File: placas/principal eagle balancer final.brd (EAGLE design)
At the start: 100 x 151 mm, 12 parts, among them X1 RJ45

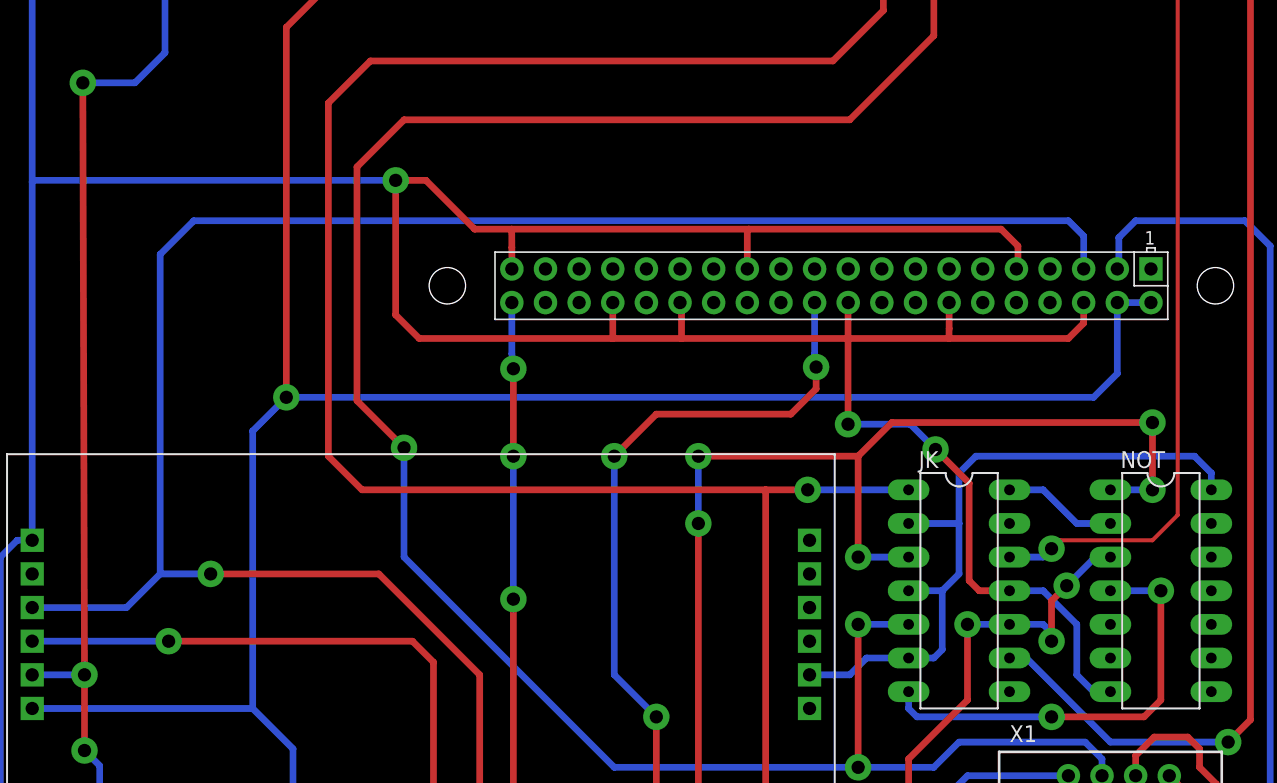
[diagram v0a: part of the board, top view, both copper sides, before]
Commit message: Versão final placa principal
Corrigidas as trilhas que levan a tensão de 3.3 a 5V nos CI 7473 e 7404
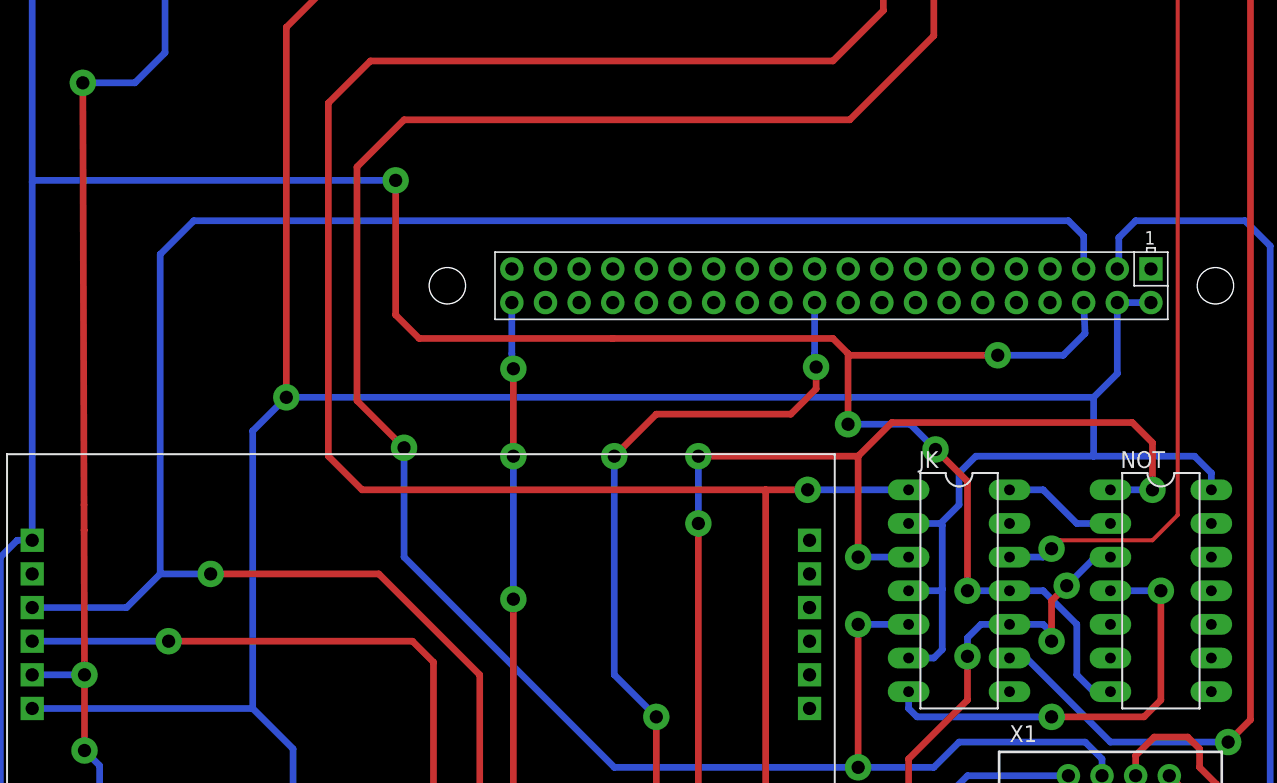
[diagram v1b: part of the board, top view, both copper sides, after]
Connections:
- net 3.3: no longer JK.2, JK.4, JK.6, NOT.14
- net 5: now also JK.2, JK.4, JK.6, NOT.14
- net GND: no longer U$2.14, U$2.20, U$2.25, U$2.30, U$2.34, U$2.39, U$2.9
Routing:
- net GND: track 578.1 -> 511.2 mm, vias 5 -> 7
- net 3.3: track 156.0 -> 103.6 mm
- net 5: track 248.7 -> 296.2 mm
- net ELCH1: track 109.6 -> 108.7 mm, vias 6 -> 5
- net ERCH1: track 51.7 -> 51.2 mm
